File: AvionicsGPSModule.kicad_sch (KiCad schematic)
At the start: 33 parts, among them P1 MC311D, Q1 AO3400A, U1 RP2040, U2 AP2112K-3.3, U3 L80-R, U4 W25Q128JVS, X1 ABM8-272-T3

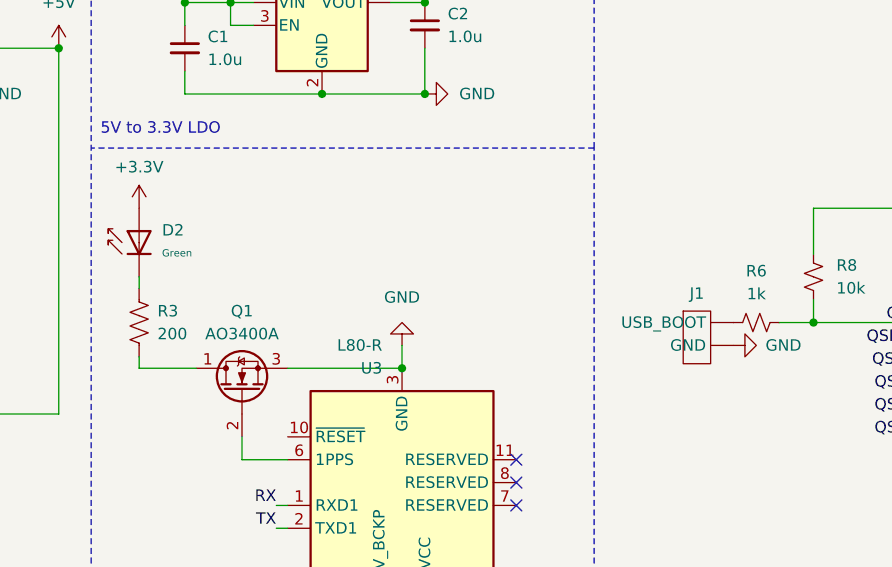
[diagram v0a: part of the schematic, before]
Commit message: Added JLC DRC requirements, and managed libraries for simpler forking
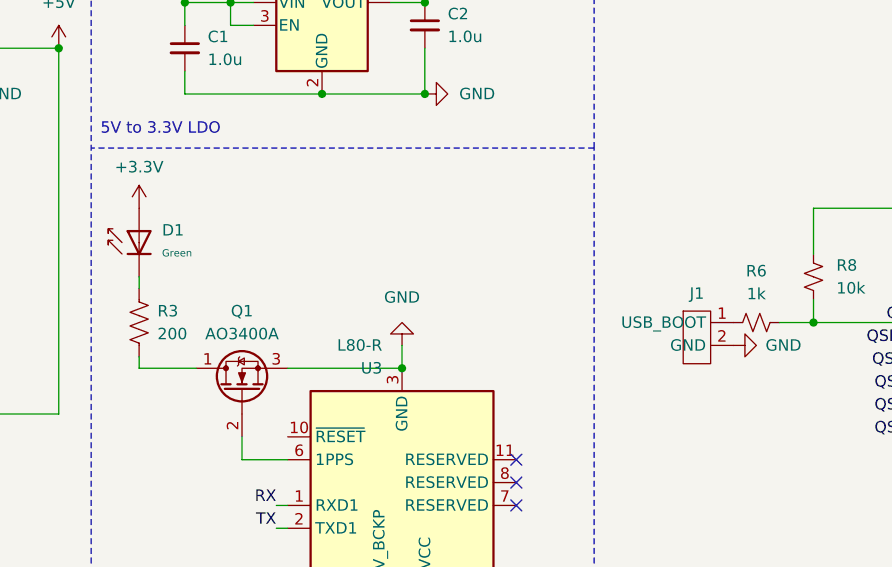
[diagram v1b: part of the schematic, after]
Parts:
- J1: footprint (none) -> Connector_PinHeader_2.54mm:PinHeader_1x02_P2.54mm_Vertical
- P1: footprint MC311D:USB-C-SMD_MC-311D -> MC-311D:USB-C-SMD_MC-311D
- X1: footprint ABM8-272-T3:ABM8-272-T3_ABR -> ABM8_272_T3:ABM8-272-T3_ABR
- renumbered D2 to D1
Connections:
- net GND: now also J1.2 (GND); no longer J1. (GND)
- net at R6.1: now also J1.1 (USB_BOOT); no longer J1. (GND)
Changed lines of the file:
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@@
 			)
 		)
-		(property "Footprint" ""
+		(property "Footprint" "Connector_PinHeader_2.54mm:PinHeader_1x02_P2.54mm_Vertical"
 			(at 139.446 64.008 0)
 			(effects
@@
 			)
 		)
-		(pin ""
-		)
-		(pin ""
+		(pin "1"
+		)
+		(pin "2"
 		)
 		(instances
@@
 			)
 		)
-		(property "Footprint" "ABM8-272-T3:ABM8-272-T3_ABR"
+		(property "Footprint" "ABM8_272_T3:ABM8-272-T3_ABR"
 			(at 153.67 116.84 0)
 			(effects
@@
 			)
 		)
-		(property "Footprint" "MC311D:USB-C-SMD_MC-311D"
+		(property "Footprint" "MC-311D:USB-C-SMD_MC-311D"
 			(at 27.686 50.8 0)
 			(effects
@@
 		(dnp no)
 		(fields_autoplaced yes)
-		(property "Reference" "D2"
+		(property "Reference" "D1"
 			(at 80.01 48.1646 0)
 			(effects
@@
 			(project ""
 				(path "/7badd1e7-b4f4-47e2-b65e-b9f9aeb44838"
-					(reference "D2")
-					(unit 1)
-				)
+					(reference "D1")
+					(unit 1)
+				)
